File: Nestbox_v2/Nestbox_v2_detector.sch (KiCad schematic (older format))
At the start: 12 parts, among them P1 CONN_01X02, P2 CONN_01X02, U1 TSOP38, U2 TSOP38

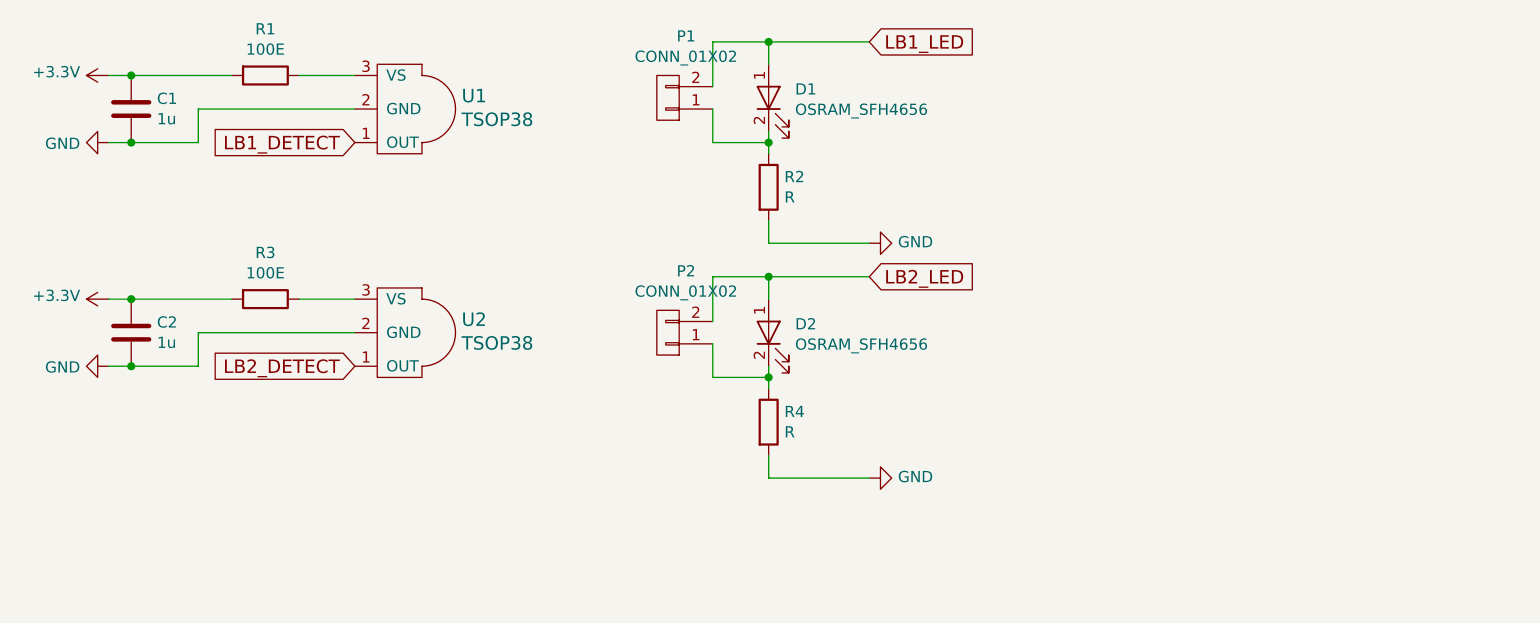
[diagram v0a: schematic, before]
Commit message: added comments for possible improvements in schematic
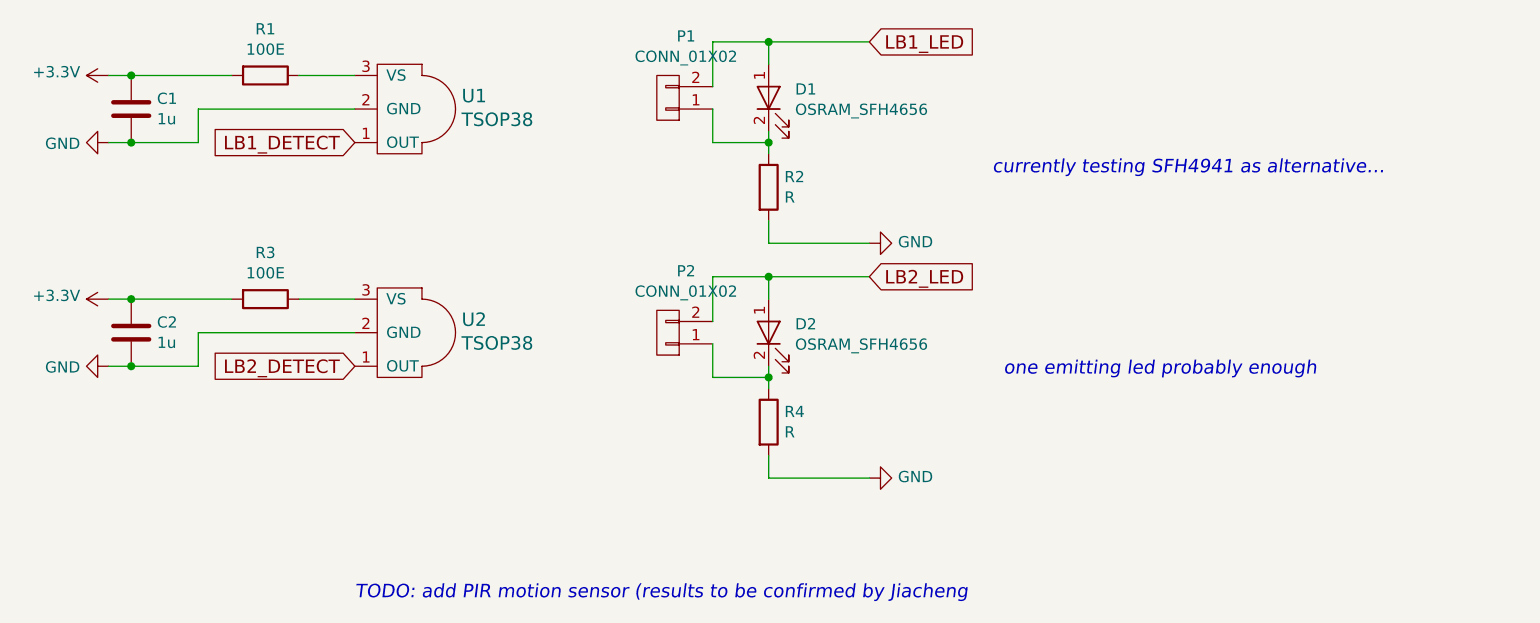
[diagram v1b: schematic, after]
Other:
- note added: "TODO: add PIR motion sensor (results to be confirmed by Jiacheng"
- note added: "currently testing SFH4941 as alternative…"
- note added: "one emitting led probably enough\n"
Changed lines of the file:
@@
 Wire Wire Line
 	2950 2750 3200 2750
+Text Notes 6050 2200 0    60   Italic 0
+currently testing SFH4941 as alternative…
+Text Notes 6100 3100 0    60   Italic 0
+one emitting led probably enough\n
+Text Notes 3200 4100 0    60   Italic 0
+TODO: add PIR motion sensor (results to be confirmed by Jiacheng
 $EndSCHEMATC
